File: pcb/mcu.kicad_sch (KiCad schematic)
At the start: 31 parts, among them J2 DEBUG, U7 ESP32-C6-WROOM-1-N8, X1 Q13FC1350000400

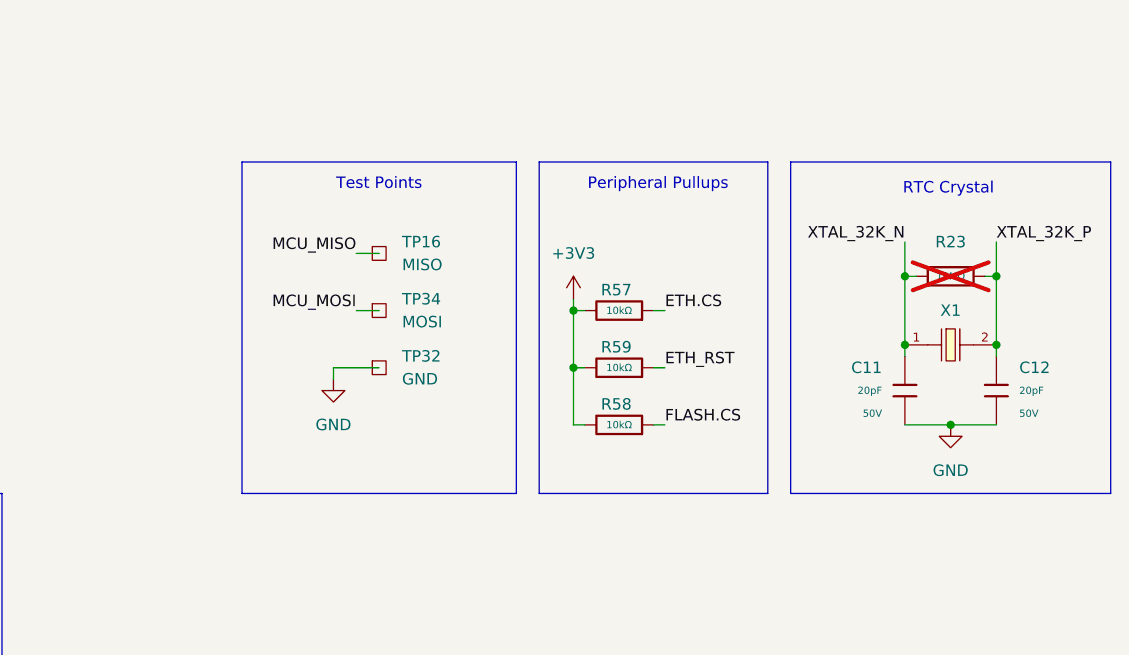
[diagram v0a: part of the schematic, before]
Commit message: sch: add frequency value to rtc crystal
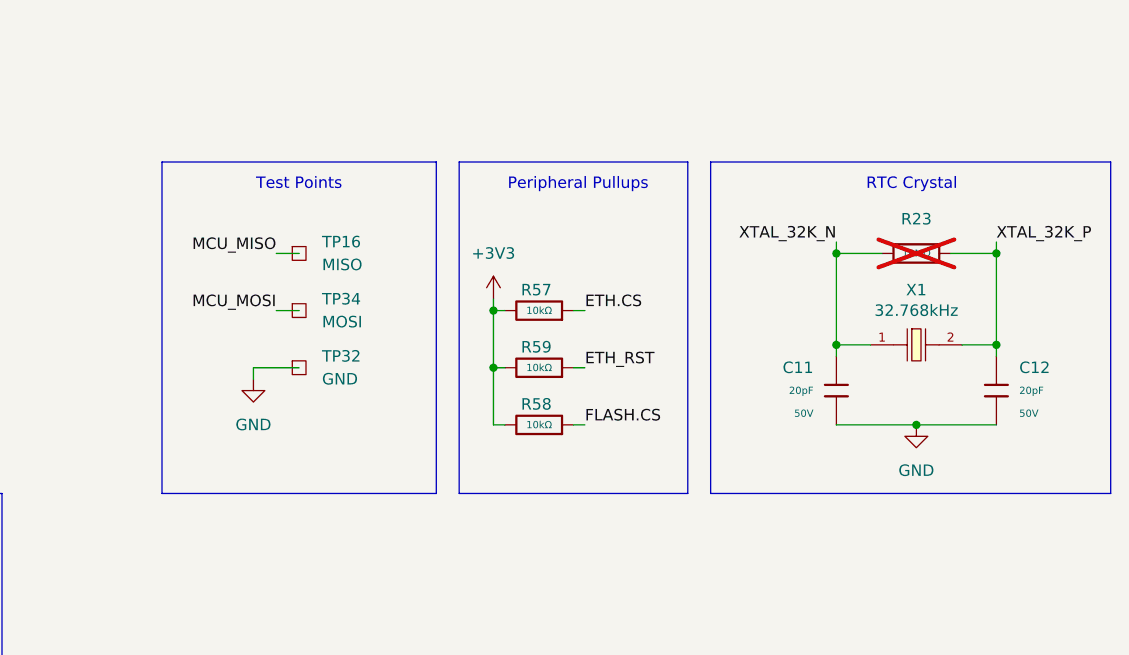
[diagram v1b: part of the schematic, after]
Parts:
- X1: value Q13FC1350000400 -> 32.768kHz
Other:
- moved on the sheet: C11, R23, R57, R58, R59, TP16, TP32, TP34, X1

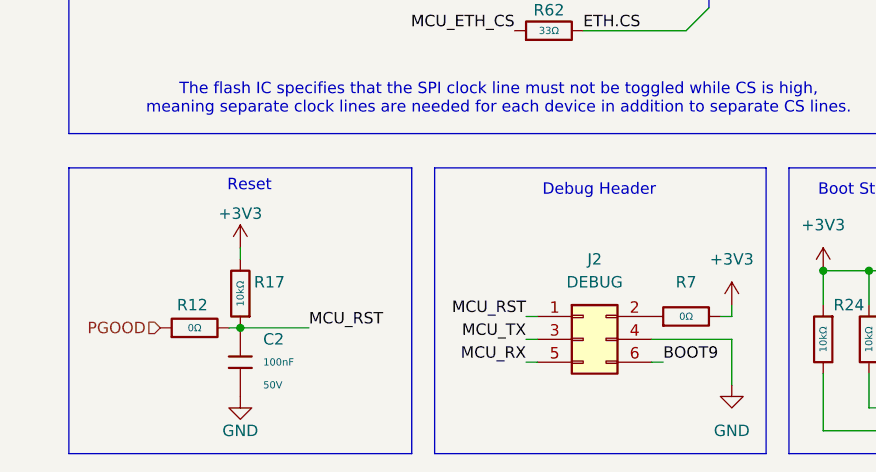
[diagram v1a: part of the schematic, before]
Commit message: pcb(mcu): route most of the esp
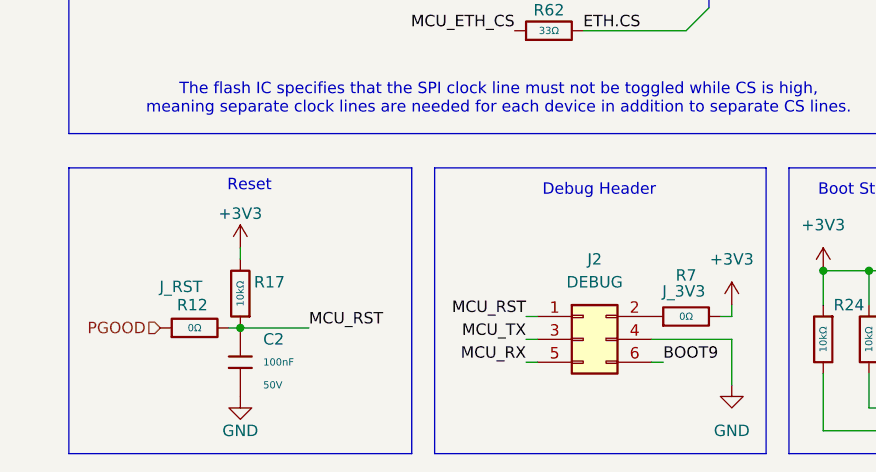
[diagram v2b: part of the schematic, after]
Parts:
- NT2: footprint (none) -> NetTie:NetTie-3_SMD_Pad0.5mm
- NT3: footprint (none) -> custom:NetTie-3_SMD_Pad0.5mm
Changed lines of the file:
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@@
 			)
 		)
-		(property "Description" "-55°C~+155°C 0Ω 100mW 75V Thick Film Resistor ±1% 0603 Chip Resistor - Surface Mount ROHS"
-			(at 29.21 180.34 0)
-			(hide yes)
+		(property "Description" "J_RST"
+			(at 27.686 175.768 90)
 			(show_name no)
 			(do_not_autoplace no)
@@
 			)
 		)
-		(property "Footprint" ""
+		(property "Footprint" "custom:NetTie-3_SMD_Pad0.5mm"
 			(at 43.18 123.19 0)
 			(hide yes)
@@
 			)
 		)
-		(property "Footprint" ""
+		(property "Footprint" "NetTie:NetTie-3_SMD_Pad0.5mm"
 			(at 46.99 130.81 0)
 			(hide yes)
@@
 		(in_pos_files yes)
 		(dnp no)
-		(fields_autoplaced yes)
 		(property "Reference" "R7"
-			(at 83.82 175.26 90)
+			(at 83.82 174.498 90)
 			(show_name no)
 			(do_not_autoplace no)
@@
 			)
 		)
-		(property "Description" "-55°C~+155°C 0Ω 100mW 75V Thick Film Resistor ±1% 0603 Chip Resistor - Surface Mount ROHS"
-			(at 83.82 179.07 0)
-			(hide yes)
+		(property "Description" "J_3V3"
+			(at 83.566 176.276 90)
 			(show_name no)
 			(do_not_autoplace no)

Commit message: pcb: route remaining tracks
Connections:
- net GND: now also U7.29 (GND)
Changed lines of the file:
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@@
 		(pin "24"
+		)
+		(pin "29"
 		)
 		(instances

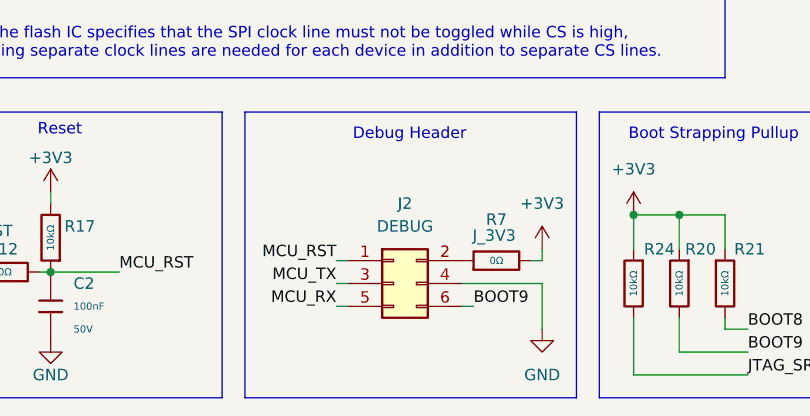
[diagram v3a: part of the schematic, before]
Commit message: pcb: fix most drc errors
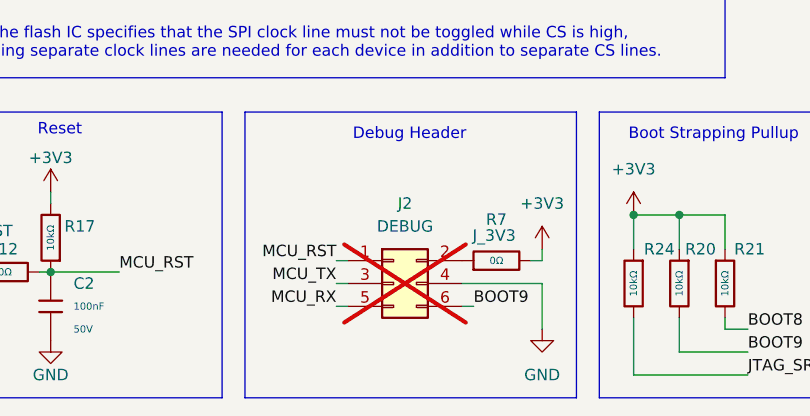
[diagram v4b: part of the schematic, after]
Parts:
- J2: now not fitted; now left out of the parts list
- TP16, TP34: footprint TestPoint:TestPoint_Pad_D1.0mm -> custom:TestPoint_Pad_D1.0mm
- TP32: footprint TestPoint:TestPoint_Plated_Hole_D2.0mm -> custom:TestPoint_Plated_Hole_D2.0mm
- X1: footprint PCM_JLCPCB:FC-135R_L3.2-W1.5 -> custom:FC-135R_L3.2-W1.5
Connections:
- net GND: now also U7.28 (GND)
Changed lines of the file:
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@@
 			)
 		)
-		(property "Footprint" "PCM_JLCPCB:FC-135R_L3.2-W1.5"
+		(property "Footprint" "custom:FC-135R_L3.2-W1.5"
 			(at 260.35 156.21 0)
 			(hide yes)
@@
 		(pin "29"
 		)
+		(pin "28"
+		)
 		(instances
 			(project "EveningStar"
@@
 			)
 		)
-		(property "Footprint" "TestPoint:TestPoint_Plated_Hole_D2.0mm"
+		(property "Footprint" "custom:TestPoint_Plated_Hole_D2.0mm"
 			(at 196.85 148.59 0)
 			(hide yes)
@@
 		(body_style 1)
 		(exclude_from_sim no)
-		(in_bom yes)
+		(in_bom no)
 		(on_board yes)
-		(in_pos_files yes)
-		(dnp no)
+		(in_pos_files no)
+		(dnp yes)
 		(fields_autoplaced yes)
 		(property "Reference" "J2"
@@
 			)
 		)
-		(property "Footprint" "TestPoint:TestPoint_Pad_D1.0mm"
+		(property "Footprint" "custom:TestPoint_Pad_D1.0mm"
 			(at 196.85 142.24 0)
 			(hide yes)
@@
 			)
 		)
-		(property "Footprint" "TestPoint:TestPoint_Pad_D1.0mm"
+		(property "Footprint" "custom:TestPoint_Pad_D1.0mm"
 			(at 196.85 135.89 0)
 			(hide yes)

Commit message: pcb(footprints): fix footprint locality
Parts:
- J2: footprint Connector_PinHeader_2.54mm:PinHeader_2x03_P2.54mm_Vertical -> custom:PinHeader_2x03_P2.54mm_Vertical
- NT2: footprint NetTie:NetTie-3_SMD_Pad0.5mm -> custom:NetTie-3_SMD_Pad0.5mm_Stock
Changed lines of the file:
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@@
 			)
 		)
-		(property "Footprint" "Connector_PinHeader_2.54mm:PinHeader_2x03_P2.54mm_Vertical"
+		(property "Footprint" "custom:PinHeader_2x03_P2.54mm_Vertical"
 			(at 72.39 181.61 0)
 			(hide yes)
@@
 			)
 		)
-		(property "Footprint" "NetTie:NetTie-3_SMD_Pad0.5mm"
+		(property "Footprint" "custom:NetTie-3_SMD_Pad0.5mm_Stock"
 			(at 46.99 130.81 0)
 			(hide yes)
